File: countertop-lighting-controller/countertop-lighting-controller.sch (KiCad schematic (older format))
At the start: 6 parts, among them P1 CONN_01X02, P2 CONN_01X03, P3 CONN_01X03, P4 CONN_01X03, U1 ESP-01v090

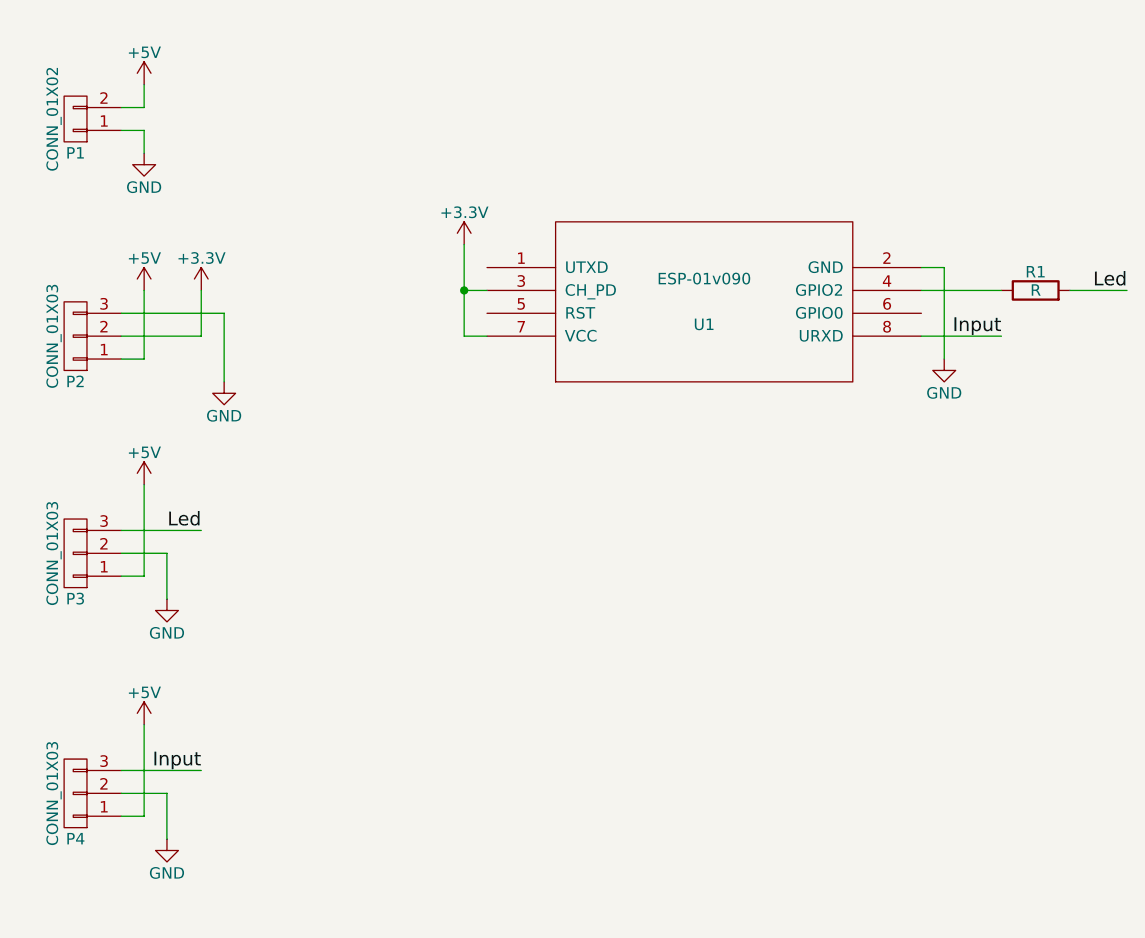
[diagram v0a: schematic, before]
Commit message: Add capacitor, change button wiring, PCB
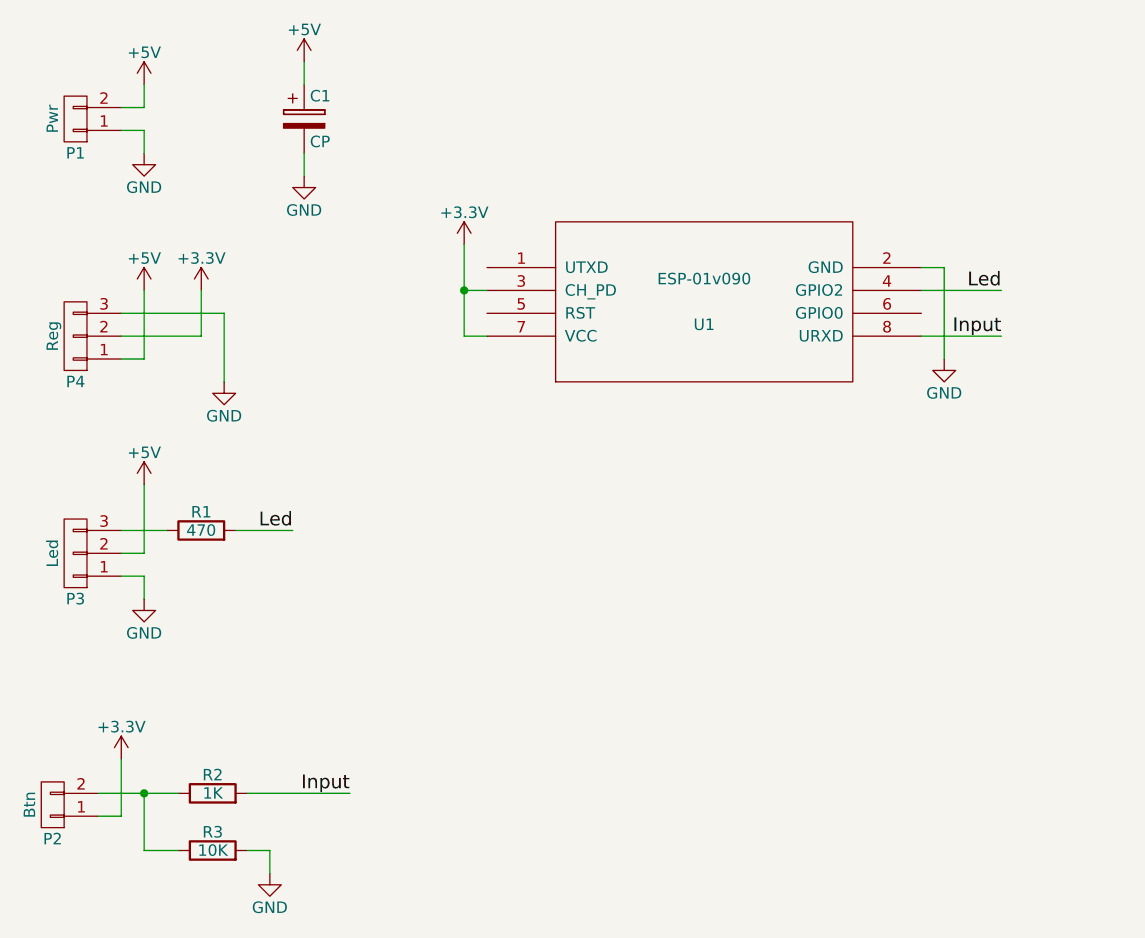
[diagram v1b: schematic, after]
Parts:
- removed P4: CONN_01X03, Pin_Headers:Pin_Header_Straight_1x03, symbol CONN_01X03
- added C1: CP, Capacitors_ThroughHole:C_Radial_D10_L16_P5, symbol CP
- added P2: Btn, Connectors_JST:JST_XH_S02B-XH-A_02x2.50mm_Angled, symbol CONN_01X02
- added R2: 1K, Resistors_SMD:R_1206_HandSoldering, symbol R
- added R3: 10K, Resistors_SMD:R_1206_HandSoldering, symbol R
- P1: value CONN_01X02 -> Pwr
- P3: value CONN_01X03 -> Led; footprint Pin_Headers:Pin_Header_Straight_1x03 -> Connectors_JST:JST_XH_S03B-XH-A_03x2.50mm_Angled
- P4: renamed from P2; value CONN_01X03 -> Reg
- R1: value R -> 470
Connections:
- net +3V3: now also P2.1 (P1)
- net +5V: now also P3.2 (P2), C1.1; no longer P3.1 (P1)
- net GND: now also P3.1 (P1), C1.2, R3.2; no longer P3.2 (P2)
- net Input: now also R2.2
- net Led: now also U1.4 (GPIO2); no longer P3.3 (P3)
- net at R1.1: now also P3.3 (P3); no longer U1.4 (GPIO2)
- new net: P2.2 (P2), R2.1, R3.1
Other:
- moved on the sheet: R1
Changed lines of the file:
@@
 P 1500 1750
 F 0 "P1" H 1500 1900 50  0000 C CNN
-F 1 "CONN_01X02" V 1600 1750 50  0000 C CNN
+F 1 "Pwr" V 1600 1750 50  0000 C CNN
 F 2 "Connect:bornier2" H 1500 1750 50  0001 C CNN
 F 3 "" H 1500 1750 50  0000 C CNN
@@
 $EndComp
 $Comp
-L GND #PWR01
+L GND #PWR2
 U 1 1 57F9436B
 P 1800 1900
-F 0 "#PWR01" H 1800 1650 50  0001 C CNN
+F 0 "#PWR2" H 1800 1650 50  0001 C CNN
 F 1 "GND" H 1800 1750 50  0000 C CNN
 F 2 "" H 1800 1900 50  0000 C CNN
@@
 $EndComp
 $Comp
-L +5V #PWR02
+L +5V #PWR1
 U 1 1 57F94383
 P 1800 1600
-F 0 "#PWR02" H 1800 1450 50  0001 C CNN
+F 0 "#PWR1" H 1800 1450 50  0001 C CNN
 F 1 "+5V" H 1800 1740 50  0000 C CNN
 F 2 "" H 1800 1600 50  0000 C CNN
@@
 $EndComp
 $Comp
-L +3.3V #PWR03
+L +3.3V #PWR7
 U 1 1 57F9439B
 P 2050 2500
-F 0 "#PWR03" H 2050 2350 50  0001 C CNN
+F 0 "#PWR7" H 2050 2350 50  0001 C CNN
 F 1 "+3.3V" H 2050 2640 50  0000 C CNN
 F 2 "" H 2050 2500 50  0000 C CNN
@@
 	1    0    0    -1
 $EndComp
-Wire Wire Line
-	1700 1700 1800 1700
-Wire Wire Line
-	1800 1700 1800 1600
-Wire Wire Line
-	1700 1800 1800 1800
-Wire Wire Line
-	1800 1800 1800 1900
-$Comp
-L CONN_01X03 P2
+$Comp
+L CONN_01X03 P4
 U 1 1 57F943BD
 P 1500 2700
-F 0 "P2" H 1500 2900 50  0000 C CNN
-F 1 "CONN_01X03" V 1600 2700 50  0000 C CNN
+F 0 "P4" H 1500 2900 50  0000 C CNN
+F 1 "Reg" V 1600 2700 50  0000 C CNN
 F 2 "Pin_Headers:Pin_Header_Straight_1x03" H 1500 2700 50  0001 C CNN
 F 3 "" H 1500 2700 50  0000 C CNN
@@
 $EndComp
 $Comp
-L +5V #PWR04
+L +5V #PWR3
 U 1 1 57F9443A
 P 1800 2500
-F 0 "#PWR04" H 1800 2350 50  0001 C CNN
+F 0 "#PWR3" H 1800 2350 50  0001 C CNN
 F 1 "+5V" H 1800 2640 50  0000 C CNN
 F 2 "" H 1800 2500 50  0000 C CNN
@@
 $EndComp
 $Comp
-L GND #PWR05
+L GND #PWR8
 U 1 1 57F94470
 P 2150 2900
-F 0 "#PWR05" H 2150 2650 50  0001 C CNN
+F 0 "#PWR8" H 2150 2650 50  0001 C CNN
 F 1 "GND" H 2150 2750 50  0000 C CNN
 F 2 "" H 2150 2900 50  0000 C CNN
@@
 	1    0    0    -1
 $EndComp
-Wire Wire Line
-	1700 2800 1800 2800
-Wire Wire Line
-	1800 2800 1800 2500
-Wire Wire Line
-	1700 2700 2050 2700
-Wire Wire Line
-	2050 2700 2050 2500
-Wire Wire Line
-	1700 2600 2150 2600
-Wire Wire Line
-	2150 2600 2150 2900
-$Comp
-L GND #PWR06
+$Comp
+L GND #PWR13
 U 1 1 57F944B3
 P 5300 2800
-F 0 "#PWR06" H 5300 2550 50  0001 C CNN
+F 0 "#PWR13" H 5300 2550 50  0001 C CNN
 F 1 "GND" H 5300 2650 50  0000 C CNN
 F 2 "" H 5300 2800 50  0000 C CNN
@@
 	1    0    0    -1
 $EndComp
-Wire Wire Line
-	5300 2800 5300 2400
-Wire Wire Line
-	5300 2400 5200 2400
-$Comp
-L +3.3V #PWR07
+$Comp
+L +3.3V #PWR12
 U 1 1 57F944F2
 P 3200 2300
-F 0 "#PWR07" H 3200 2150 50  0001 C CNN
+F 0 "#PWR12" H 3200 2150 50  0001 C CNN
 F 1 "+3.3V" H 3200 2440 50  0000 C CNN
 F 2 "" H 3200 2300 50  0000 C CNN
@@
 	1    0    0    -1
 $EndComp
-Wire Wire Line
-	3200 2300 3200 2700
-Wire Wire Line
-	3200 2700 3300 2700
-Wire Wire Line
-	3300 2500 3200 2500
-Connection ~ 3200 2500
-$Comp
-L +5V #PWR08
+$Comp
+L +5V #PWR4
 U 1 1 57F9465C
 P 1800 3350
-F 0 "#PWR08" H 1800 3200 50  0001 C CNN
+F 0 "#PWR4" H 1800 3200 50  0001 C CNN
 F 1 "+5V" H 1800 3490 50  0000 C CNN
 F 2 "" H 1800 3350 50  0000 C CNN
@@
 $EndComp
 $Comp
-L GND #PWR09
+L GND #PWR6
 U 1 1 57F94673
-P 1900 3850
-F 0 "#PWR09" H 1900 3600 50  0001 C CNN
-F 1 "GND" H 1900 3700 50  0000 C CNN
-F 2 "" H 1900 3850 50  0000 C CNN
-F 3 "" H 1900 3850 50  0000 C CNN
-	1    1900 3850
-	1    0    0    -1
-$EndComp
-Wire Wire Line
-	1700 3750 1800 3750
-Wire Wire Line
-	1800 3750 1800 3350
-Wire Wire Line
-	1700 3650 1900 3650
-Wire Wire Line
-	1900 3650 1900 3850
-Text Label 2050 3550 2    60   ~ 0
+P 1800 3850
+F 0 "#PWR6" H 1800 3600 50  0001 C CNN
+F 1 "GND" H 1800 3700 50  0000 C CNN
+F 2 "" H 1800 3850 50  0000 C CNN
+F 3 "" H 1800 3850 50  0000 C CNN
+	1    1800 3850
+	1    0    0    -1
+$EndComp
+Text Label 2450 3550 2    60   ~ 0
 Led
-Wire Wire Line
-	2050 3550 1700 3550
-Text Label 6100 2500 2    60   ~ 0
+Text Label 5550 2500 2    60   ~ 0
 Led
 Text Label 5550 2700 2    60   ~ 0
 Input
-Wire Wire Line
-	5550 2700 5200 2700
-Wire Wire Line
-	5550 2500 5200 2500
 $Comp
 L R R1
 U 1 1 57F949E7
-P 5700 2500
-F 0 "R1" V 5780 2500 50  0000 C CNN
-F 1 "R" V 5700 2500 50  0000 C CNN
-F 2 "Resistors_SMD:R_1206_HandSoldering" V 5630 2500 50  0001 C CNN
-F 3 "" H 5700 2500 50  0000 C CNN
-	1    5700 2500
+P 2050 3550
+F 0 "R1" V 2130 3550 50  0000 C CNN
+F 1 "470" V 2050 3550 50  0000 C CNN
+F 2 "Resistors_SMD:R_1206_HandSoldering" V 1980 3550 50  0001 C CNN
+F 3 "" H 2050 3550 50  0000 C CNN
+	1    2050 3550
 	0    -1   -1   0
 $EndComp
-Wire Wire Line
-	6100 2500 5850 2500
 $Comp
 L CONN_01X03 P3
@@
 P 1500 3650
 F 0 "P3" H 1500 3850 50  0000 C CNN
-F 1 "CONN_01X03" V 1600 3650 50  0000 C CNN
-F 2 "Pin_Headers:Pin_Header_Straight_1x03" H 1500 3650 50  0001 C CNN
+F 1 "Led" V 1600 3650 50  0000 C CNN
+F 2 "Connectors_JST:JST_XH_S03B-XH-A_03x2.50mm_Angled" H 1500 3650 50  0001 C CNN
 F 3 "" H 1500 3650 50  0000 C CNN
 	1    1500 3650
@@
 $EndComp
 $Comp
-L +5V #PWR010
-U 1 1 57F94F66
-P 1800 4400
-F 0 "#PWR010" H 1800 4250 50  0001 C CNN
-F 1 "+5V" H 1800 4540 50  0000 C CNN
-F 2 "" H 1800 4400 50  0000 C CNN
-F 3 "" H 1800 4400 50  0000 C CNN
-	1    1800 4400
-	1    0    0    -1
-$EndComp
-$Comp
-L GND #PWR011
+L GND #PWR9
 U 1 1 57F94F6C
-P 1900 4900
-F 0 "#PWR011" H 1900 4650 50  0001 C CNN
-F 1 "GND" H 1900 4750 50  0000 C CNN
-F 2 "" H 1900 4900 50  0000 C CNN
-F 3 "" H 1900 4900 50  0000 C CNN
-	1    1900 4900
-	1    0    0    -1
-$EndComp
-Wire Wire Line
-	1700 4800 1800 4800
-Wire Wire Line
-	1800 4800 1800 4400
-Wire Wire Line
-	1700 4700 1900 4700
-Wire Wire Line
-	1900 4700 1900 4900
-Text Label 2050 4600 2    60   ~ 0
+P 2350 5050
+F 0 "#PWR9" H 2350 4800 50  0001 C CNN
+F 1 "GND" H 2350 4900 50  0000 C CNN
+F 2 "" H 2350 5050 50  0000 C CNN
+F 3 "" H 2350 5050 50  0000 C CNN
+	1    2350 5050
+	1    0    0    -1
+$EndComp
+Text Label 2700 4700 2    60   ~ 0
 Input
-Wire Wire Line
-	2050 4600 1700 4600
-$Comp
-L CONN_01X03 P4
-U 1 1 57F94F78
-P 1500 4700
-F 0 "P4" H 1500 4900 50  0000 C CNN
-F 1 "CONN_01X03" V 1600 4700 50  0000 C CNN
-F 2 "Pin_Headers:Pin_Header_Straight_1x03" H 1500 4700 50  0001 C CNN
-F 3 "" H 1500 4700 50  0000 C CNN
-	1    1500 4700
+$Comp
+L +3.3V #PWR5
+U 1 1 57F96769
+P 1700 4550
+F 0 "#PWR5" H 1700 4400 50  0001 C CNN
+F 1 "+3.3V" H 1700 4690 50  0000 C CNN
+F 2 "" H 1700 4550 50  0000 C CNN
+F 3 "" H 1700 4550 50  0000 C CNN
+	1    1700 4550
+	1    0    0    -1
+$EndComp
+$Comp
+L CONN_01X02 P2
+U 1 1 580B965D
+P 1400 4750
+F 0 "P2" H 1400 4900 50  0000 C CNN
+F 1 "Btn" V 1500 4750 50  0000 C CNN
+F 2 "Connectors_JST:JST_XH_S02B-XH-A_02x2.50mm_Angled" H 1400 4750 50  0001 C CNN
+F 3 "" H 1400 4750 50  0000 C CNN
+	1    1400 4750
 	-1   0    0    1
 $EndComp
+$Comp
+L R R2
+U 1 1 580B98B5
+P 2100 4700
+F 0 "R2" V 2180 4700 50  0000 C CNN
+F 1 "1K" V 2100 4700 50  0000 C CNN
+F 2 "Resistors_SMD:R_1206_HandSoldering" V 2030 4700 50  0001 C CNN
+F 3 "" H 2100 4700 50  0000 C CNN
+	1    2100 4700
+	0    -1   -1   0
+$EndComp
+$Comp
+L R R3
+U 1 1 580B9AE6
+P 2100 4950
+F 0 "R3" V 2180 4950 50  0000 C CNN
+F 1 "10K" V 2100 4950 50  0000 C CNN
+F 2 "Resistors_SMD:R_1206_HandSoldering" V 2030 4950 50  0001 C CNN
+F 3 "" H 2100 4950 50  0000 C CNN
+	1    2100 4950
+	0    -1   -1   0
+$EndComp
+$Comp
+L CP C1
+U 1 1 580BA2A9
+P 2500 1750
+F 0 "C1" H 2525 1850 50  0000 L CNN
+F 1 "CP" H 2525 1650 50  0000 L CNN
+F 2 "Capacitors_ThroughHole:C_Radial_D10_L16_P5" H 2538 1600 50  0001 C CNN
+F 3 "" H 2500 1750 50  0000 C CNN
+	1    2500 1750
+	1    0    0    -1
+$EndComp
+$Comp
+L +5V #PWR10
+U 1 1 580BA32F
+P 2500 1500
+F 0 "#PWR10" H 2500 1350 50  0001 C CNN
+F 1 "+5V" H 2500 1640 50  0000 C CNN
+F 2 "" H 2500 1500 50  0000 C CNN
+F 3 "" H 2500 1500 50  0000 C CNN
+	1    2500 1500
+	1    0    0    -1
+$EndComp
+$Comp
+L GND #PWR11
+U 1 1 580BA355
+P 2500 2000
+F 0 "#PWR11" H 2500 1750 50  0001 C CNN
+F 1 "GND" H 2500 1850 50  0000 C CNN
+F 2 "" H 2500 2000 50  0000 C CNN
+F 3 "" H 2500 2000 50  0000 C CNN
+	1    2500 2000
+	1    0    0    -1
+$EndComp
+Wire Wire Line
+	1700 1700 1800 1700
+Wire Wire Line
+	1800 1700 1800 1600
+Wire Wire Line
+	1700 1800 1800 1800
+Wire Wire Line
+	1800 1800 1800 1900
+Wire Wire Line
+	1700 2800 1800 2800
+Wire Wire Line
+	1800 2800 1800 2500
+Wire Wire Line
+	1700 2700 2050 2700
+Wire Wire Line
+	2050 2700 2050 2500
+Wire Wire Line
+	1700 2600 2150 2600
+Wire Wire Line
+	2150 2600 2150 2900
+Wire Wire Line
+	5300 2800 5300 2400
+Wire Wire Line
+	5300 2400 5200 2400
+Wire Wire Line
+	3200 2300 3200 2700
+Wire Wire Line
+	3200 2700 3300 2700
+Wire Wire Line
+	3300 2500 3200 2500
+Connection ~ 3200 2500
+Wire Wire Line
+	5550 2700 5200 2700
+Wire Wire Line
+	5550 2500 5200 2500
+Wire Wire Line
+	1600 4700 1950 4700
+Wire Wire Line
+	2250 4700 2700 4700
+Wire Wire Line
+	2250 4950 2350 4950
+Wire Wire Line
+	2350 4950 2350 5050
+Wire Wire Line
+	1950 4950 1800 4950
+Wire Wire Line
+	1800 4950 1800 4700
+Connection ~ 1800 4700
+Wire Wire Line
+	1700 3550 1900 3550
+Wire Wire Line
+	2450 3550 2200 3550
+Wire Wire Line
+	2500 1500 2500 1600
+Wire Wire Line
+	2500 1900 2500 2000
+Wire Wire Line
+	1700 3750 1800 3750
+Wire Wire Line
+	1800 3750 1800 3850
+Wire Wire Line
+	1700 3650 1800 3650
+Wire Wire Line
+	1800 3650 1800 3350
+Wire Wire Line
+	1700 4550 1700 4800
+Wire Wire Line
+	1700 4800 1600 4800
 $EndSCHEMATC
